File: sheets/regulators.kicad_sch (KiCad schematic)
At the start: 0 parts

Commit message: Schematic capture: power entry (p2) and regulators (p3)
Pages 2 and 3 drawn to the schematic rules adopted on 2026-10-22 (wired
clusters in dashed boxes, labels only between clusters and sheets, one
rail symbol per cluster, every net named, D-45 values with separate
voltage/tolerance/dielectric fields). Design values and their reasons
are on each sheet. Parts not yet in the DropOut library are stock
Device symbols marked PLACEHOLDER with empty MPN fields.

The root index now carries the sheet interfaces as sheet pins, laid out
along the power and signal path. check_schematic.py also fails on
auto-generated net names (rule O-2). CLAUDE.md records the four project
answers and the net-naming decisions.

Co-Authored-By: Claude Opus 5.5 <noreply@anthropic.com>
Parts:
- added C (x4): 4.7uF, symbol Device:C
- added C (x4): 1uF, symbol Device:C
- added C (x5): 22uF, symbol Device:C
- added C (x5): 100nF, symbol Device:C
- added L: 2.2uH, symbol Device:L
- added L: 1uH, symbol Device:L
- added R (x2): 100k, symbol Device:R
- added R (x3): 0R, symbol Device:R
- added R: 28k, symbol Device:R
- added R: 14k, symbol Device:R
- added R: 4.7k, symbol Device:R
- added TP: TP_VDDAU_AON, symbol Connector:TestPoint
- added TP: TP_1V5_CORE, symbol Connector:TestPoint
- added TP: TP_3V3_MAIN, symbol Connector:TestPoint
- added TP: TP_INH, symbol Connector:TestPoint
- added TP: TP_GND, symbol Connector:TestPoint
- added TP: TP_1V5_EN, symbol Connector:TestPoint
- added TP: TP_VBAT_FILT, symbol Connector:TestPoint
- added TP: TP_RESET_L, symbol Connector:TestPoint
- added U: TPS3702AX33QDDCRQ1, DropOut_Package_TO_SOT_SMD:Texas_DDC0006A_TSOT-23-6, symbol DropOut_Power:TPS3702AX33QDDCRQ1
- added U (x2): LMQ66430MC3RXBRQ1, DropOut_Package_DFN_QFN:Texas_RXB0014A_VQFN-14-1EP_2.6x2.6mm_P0.5mm_EP1x1mm, symbol DropOut_Power:LMQ66430MC3RXBRQ1
- added U: LDO, symbol Connector_Generic:Conn_01x04
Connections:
- new net 1V5_CORE: R.2, TP.1
- new net 1V5_CORE_FB: R.1, R.2, U.11 (VOUT/FB)
- new net 1V5_CORE_REG: C.1, C.1, C.1, C.1, L.2, R.1, R.1
- new net 1V5_CORE_SW: L.1, U.7 (SW)
- new net 1V5_CORE_VCC: C.1, U.10 (VCC)
- new net 1V5_EN: R.1, R.2, TP.1, U.1 (EN/UVLO)
- new net 3V3_MAIN: C.1, R.1, R.1, R.2, TP.1, U.3 (SENSE), U.5 (VDD)
- new net 3V3_MAIN_REG: C.1, C.1, C.1, L.2, R.1, U.11 (VOUT/FB)
- new net 3V3_MAIN_SW: L.1, U.7 (SW)
- new net 3V3_MAIN_VCC: C.1, U.10 (VCC)
- new net GND: C.2, C.2, C.2, C.2, C.2, C.2, C.2, C.2, C.2, C.2, C.2, C.2, C.2, C.2, C.2, C.2, C.2, C.2, R.2, R.2, TP.1, U.13 (MODE/SYNC), U.13 (MODE/SYNC), U.15 (GND), U.15 (GND), U.2 (GND), U.4 (Pin_4), U.4 (SET), U.6 (PGND), U.6 (PGND)
- new net INH: TP.1, U.1 (EN/UVLO)
- new net RESET_L: R.2, TP.1, U.1 (~{UV}), U.6 (~{OV})
- new net VBAT_FILT: C.1, C.1, C.1, C.1, C.1, C.1, TP.1, U.3 (VIN), U.3 (VIN)
- new net VBAT_PROT: C.1, U.1 (Pin_1), U.2 (Pin_2)
- new net VDDAU_AON: R.2, TP.1
- new net VDDAU_AON_REG: C.1, R.1, U.3 (Pin_3)
- no-connect marks 0 -> 14
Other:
- note added: "1V5 EN chain (R3xx)"
- note added: "1V5_CORE buck, EN chained from 3V3_MAIN (U303, L302)"
- note added: "3V3_MAIN buck, enabled by LAN8670 INH (U302, L301)"
- note added: "3V3_MAIN window supervisor to RESET_L (U304)"
- note added: "Always-on LAN8670 VDDAU supply: nanopower LDO, PLACEHOLDER (U301)"
- note added: "DESIGN VALUES (LMQ66430-Q1 SNVSBV1F; TPS3702-Q1 SBVS261C; Node60 DEC-004, DEC-006). Values per D-45. Power-up order (DEC-004): VDDAU_AON always on -> LAN8670 INH high -> U302 3V3_MAIN -> 3V3_MAIN > 2.46 V -> U303 1V5_CORE. VDDA <= VDDAU + 0.5 V holds because VDDAU is up first. No FS26, latch or MCU gate. 0R debug links (project default: every regulator output): R on each *_REG -> rail, 0603 rated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"
- note added: "Power flags (ERC)"
- note added: "Test points"
- title: Node60 -> Node60 · B · Regulators (p3)

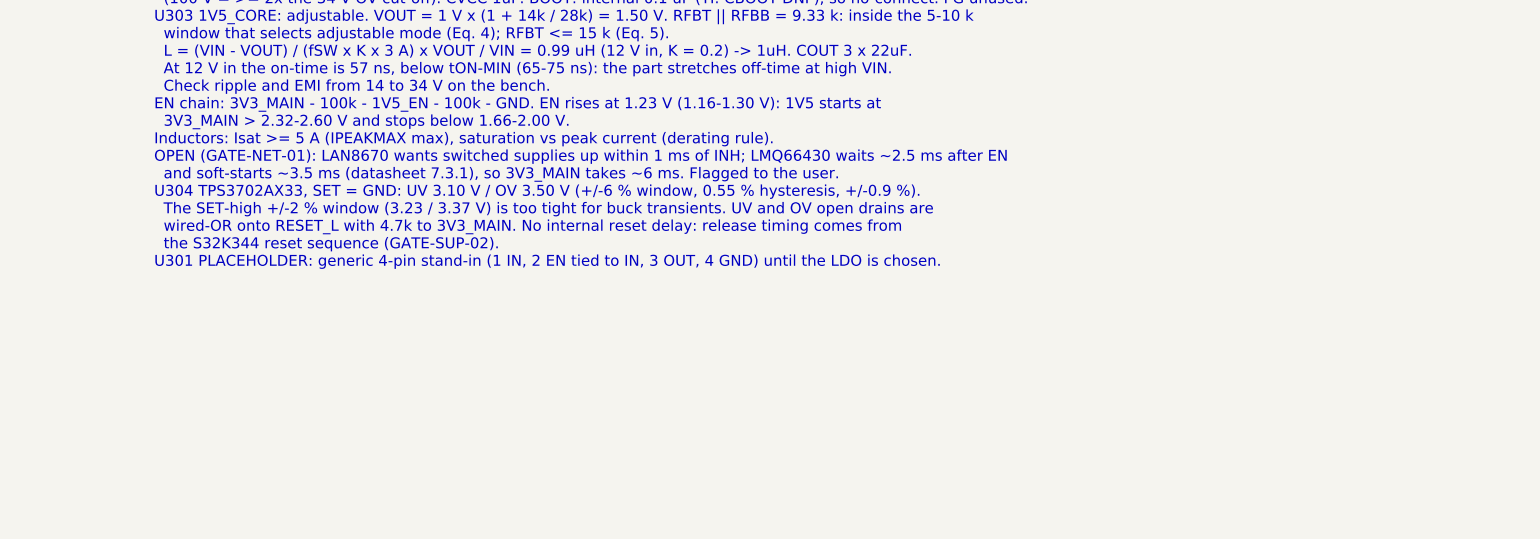
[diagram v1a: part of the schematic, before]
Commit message: Record TBD part selections; schematic follows them
User selections of 2026-10-22: TPS7B8133QWDRVRQ1 (VDDAU LDO),
CSS2725FTL250 (0.25 mOhm RSENSE), IAUTN08S5N012LATMA1 (DGATE/HGATE
FETs, new parts entry) and NCU18XH103F6SRB (NTCs), each with its dated
DigiKey observation and the rejected or alternative candidates, which
are now parts entries too. The schematic placeholders carry the
selected MPNs until the library parts land. CCAP grows to 1uF:
10 x the summed Ciss of four IAUTN08S5N012L is 0.61 uF.

Co-Authored-By: Claude Opus 5.5 <noreply@anthropic.com>
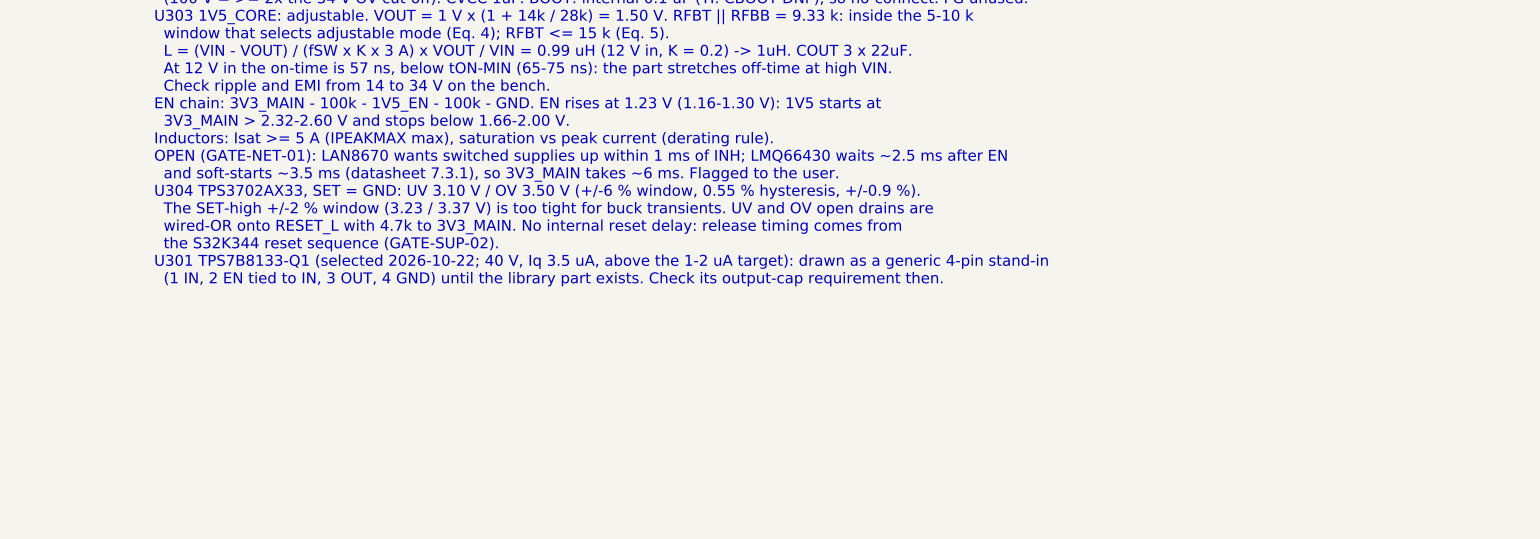
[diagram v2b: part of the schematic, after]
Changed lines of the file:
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@@
 		)
 	)
-	(text "DESIGN VALUES (LMQ66430-Q1 SNVSBV1F; TPS3702-Q1 SBVS261C; Node60 DEC-004, DEC-006). Values per D-45.\nPower-up order (DEC-004): VDDAU_AON always on -> LAN8670 INH high -> U302 3V3_MAIN -> 3V3_MAIN > 2.46 V\n  -> U303 1V5_CORE. VDDA <= VDDAU + 0.5 V holds because VDDAU is up first. No FS26, latch or MCU gate.\n0R debug links (project default: every regulator output): R on each *_REG -> rail, 0603 rated 2 A.\n  Feedback senses the regulator side, so opening the link leaves the regulator in regulation.\nU302 3V3_MAIN: LMQ66430MC3 fixed 3.3 V (VOUT/FB on the output), 2.2 MHz, MODE/SYNC = GND (auto PFM/PWM).\n  TI Table 8-4: L 2.2uH, COUT >= 40 uF effective -> 2 x 22uF 10V 1210 + 100nF; CIN 2 x 4.7uF 100V + 100nF 100V\n  (100 V = >= 2x the 34 V OV cut-off). CVCC 1uF. BOOT: internal 0.1 uF (TI: CBOOT DNP), so no-connect. PG unused.\nU303 1V5_CORE: adjustable. VOUT = 1 V x (1 + 14k / 28k) = 1.50 V. RFBT || RFBB = 9.33 k: inside the 5-10 k\n  window that selects adjustable mode (Eq. 4); RFBT <= 15 k (Eq. 5).\n  L = (VIN - VOUT) / (fSW x K x 3 A) x VOUT / VIN = 0.99 uH (12 V in, K = 0.2) -> 1uH. COUT 3 x 22uF.\n  At 12 V in the on-time is 57 ns, below tON-MIN (65-75 ns): the part stretches off-time at high VIN.\n  Check ripple and EMI from 14 to 34 V on the bench.\nEN chain: 3V3_MAIN - 100k - 1V5_EN - 100k - GND. EN rises at 1.23 V (1.16-1.30 V): 1V5 starts at\n  3V3_MAIN > 2.32-2.60 V and stops below 1.66-2.00 V.\nInductors: Isat >= 5 A (IPEAKMAX max), saturation vs peak current (derating rule).\nOPEN (GATE-NET-01): LAN8670 wants switched supplies up within 1 ms of INH; LMQ66430 waits ~2.5 ms after EN\n  and soft-starts ~3.5 ms (datasheet 7.3.1), so 3V3_MAIN takes ~6 ms. Flagged to the user.\nU304 TPS3702AX33, SET = GND: UV 3.10 V / OV 3.50 V (+/-6 % window, 0.55 % hysteresis, +/-0.9 %).\n  The SET-high +/-2 % window (3.23 / 3.37 V) is too tight for buck transients. UV and OV open drains are\n  wired-OR onto RESET_L with 4.7k to 3V3_MAIN. No internal reset delay: release timing comes from\n  the S32K344 reset sequence (GATE-SUP-02).\nU301 PLACEHOLDER: generic 4-pin stand-in (1 IN, 2 EN tied to IN, 3 OUT, 4 GND) until the LDO is chosen.\n"
+	(text "DESIGN VALUES (LMQ66430-Q1 SNVSBV1F; TPS3702-Q1 SBVS261C; Node60 DEC-004, DEC-006). Values per D-45.\nPower-up order (DEC-004): VDDAU_AON always on -> LAN8670 INH high -> U302 3V3_MAIN -> 3V3_MAIN > 2.46 V\n  -> U303 1V5_CORE. VDDA <= VDDAU + 0.5 V holds because VDDAU is up first. No FS26, latch or MCU gate.\n0R debug links (project default: every regulator output): R on each *_REG -> rail, 0603 rated 2 A.\n  Feedback senses the regulator side, so opening the link leaves the regulator in regulation.\nU302 3V3_MAIN: LMQ66430MC3 fixed 3.3 V (VOUT/FB on the output), 2.2 MHz, MODE/SYNC = GND (auto PFM/PWM).\n  TI Table 8-4: L 2.2uH, COUT >= 40 uF effective -> 2 x 22uF 10V 1210 + 100nF; CIN 2 x 4.7uF 100V + 100nF 100V\n  (100 V = >= 2x the 34 V OV cut-off). CVCC 1uF. BOOT: internal 0.1 uF (TI: CBOOT DNP), so no-connect. PG unused.\nU303 1V5_CORE: adjustable. VOUT = 1 V x (1 + 14k / 28k) = 1.50 V. RFBT || RFBB = 9.33 k: inside the 5-10 k\n  window that selects adjustable mode (Eq. 4); RFBT <= 15 k (Eq. 5).\n  L = (VIN - VOUT) / (fSW x K x 3 A) x VOUT / VIN = 0.99 uH (12 V in, K = 0.2) -> 1uH. COUT 3 x 22uF.\n  At 12 V in the on-time is 57 ns, below tON-MIN (65-75 ns): the part stretches off-time at high VIN.\n  Check ripple and EMI from 14 to 34 V on the bench.\nEN chain: 3V3_MAIN - 100k - 1V5_EN - 100k - GND. EN rises at 1.23 V (1.16-1.30 V): 1V5 starts at\n  3V3_MAIN > 2.32-2.60 V and stops below 1.66-2.00 V.\nInductors: Isat >= 5 A (IPEAKMAX max), saturation vs peak current (derating rule).\nOPEN (GATE-NET-01): LAN8670 wants switched supplies up within 1 ms of INH; LMQ66430 waits ~2.5 ms after EN\n  and soft-starts ~3.5 ms (datasheet 7.3.1), so 3V3_MAIN takes ~6 ms. Flagged to the user.\nU304 TPS3702AX33, SET = GND: UV 3.10 V / OV 3.50 V (+/-6 % window, 0.55 % hysteresis, +/-0.9 %).\n  The SET-high +/-2 % window (3.23 / 3.37 V) is too tight for buck transients. UV and OV open drains are\n  wired-OR onto RESET_L with 4.7k to 3V3_MAIN. No internal reset delay: release timing comes from\n  the S32K344 reset sequence (GATE-SUP-02).\nU301 TPS7B8133-Q1 (selected 2026-10-22; 40 V, Iq 3.5 uA, above the 1-2 uA target): drawn as a generic 4-pin stand-in\n  (1 IN, 2 EN tied to IN, 3 OUT, 4 GND) until the library part exists. Check its output-cap requirement then.\n"
 		(exclude_from_sim no)
 		(at 330.2 40.64 0)
